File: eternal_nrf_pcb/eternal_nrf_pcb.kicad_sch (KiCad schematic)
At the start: 19 parts, among them U1 BQ25504

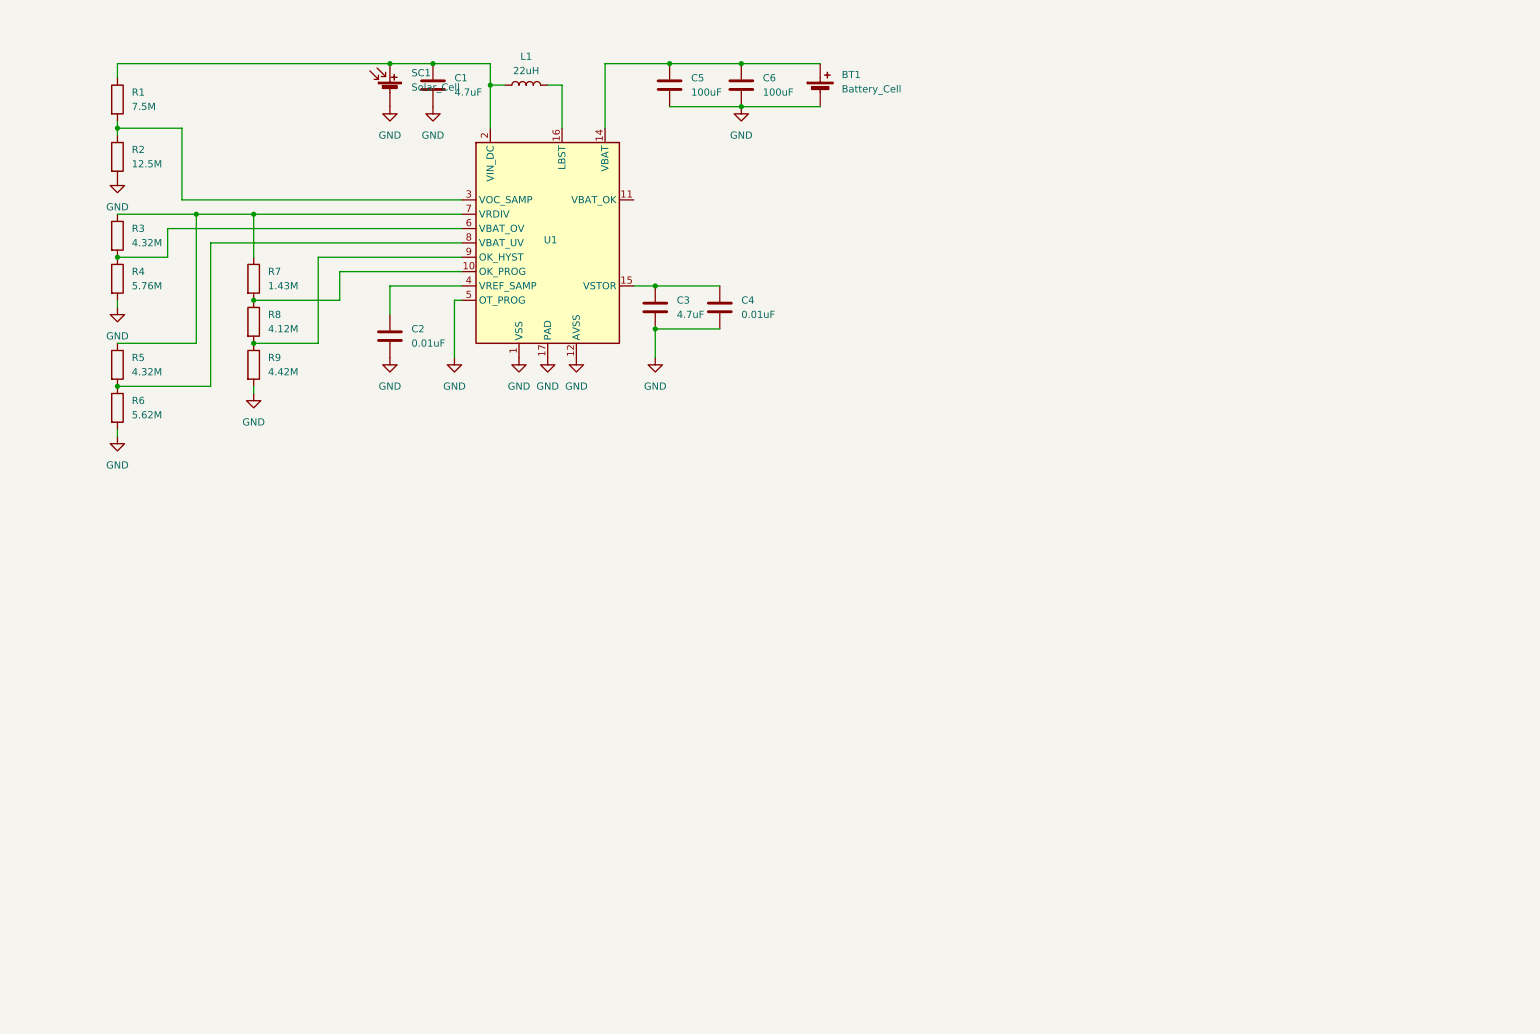
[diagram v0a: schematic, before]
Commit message: add nrf barebones schema
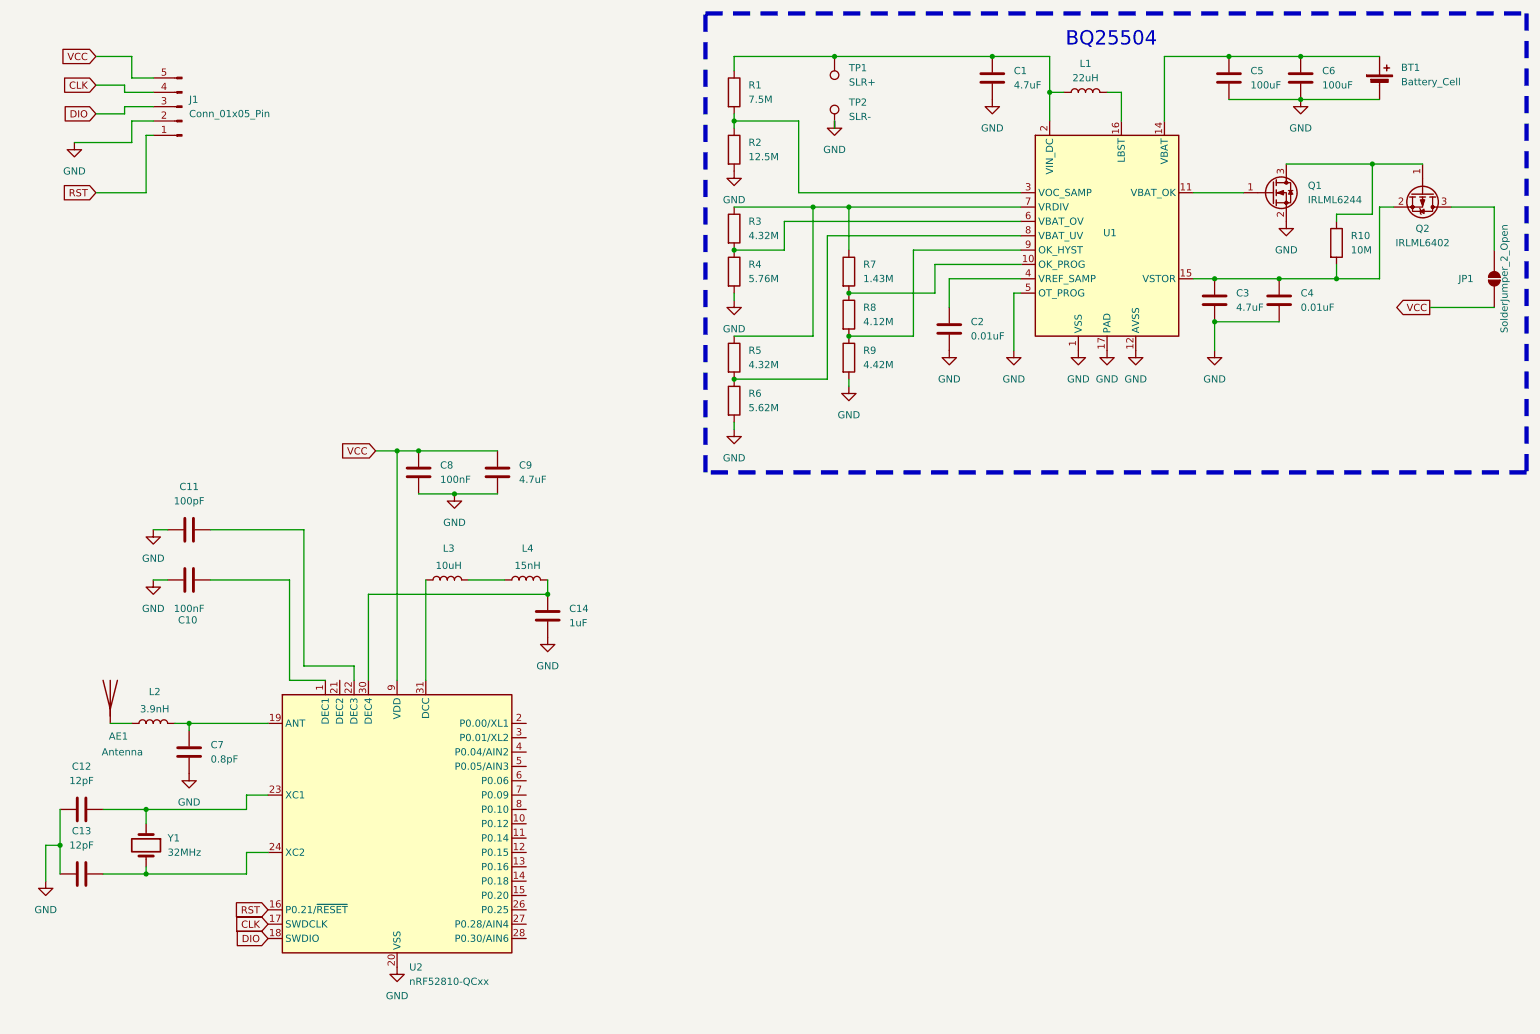
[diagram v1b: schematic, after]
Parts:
- removed SC1: Solar_Cell, symbol Device:Solar_Cell
- added AE1: Antenna, symbol Device:Antenna
- added C10, C8: 100nF, Capacitor_SMD:C_0402_1005Metric_Pad0.74x0.62mm_HandSolder, symbol Device:C
- added C11: 100pF, Capacitor_SMD:C_0402_1005Metric_Pad0.74x0.62mm_HandSolder, symbol Device:C
- added C12, C13: 12pF, Capacitor_SMD:C_0402_1005Metric_Pad0.74x0.62mm_HandSolder, symbol Device:C
- added C14: 1uF, Capacitor_SMD:C_0402_1005Metric_Pad0.74x0.62mm_HandSolder, symbol Device:C
- added C7: 0.8pF, Capacitor_SMD:C_0402_1005Metric_Pad0.74x0.62mm_HandSolder, symbol Device:C
- added C9: 4.7uF, Capacitor_SMD:C_0603_1608Metric_Pad1.08x0.95mm_HandSolder, symbol Device:C
- added J1: Conn_01x05_Pin, Connector_PinHeader_2.00mm:PinHeader_1x05_P2.00mm_Vertical, symbol Connector:Conn_01x05_Pin
- added JP1: SolderJumper_2_Open, Jumper:SolderJumper-2_P1.3mm_Open_TrianglePad1.0x1.5mm, symbol Jumper:SolderJumper_2_Open
- added L2: 3.9nH, Inductor_SMD:L_0402_1005Metric_Pad0.77x0.64mm_HandSolder, symbol Device:L
- added L3: 10uH, Inductor_SMD:L_0603_1608Metric_Pad1.05x0.95mm_HandSolder, symbol Device:L
- added L4: 15nH, Inductor_SMD:L_0402_1005Metric_Pad0.77x0.64mm_HandSolder, symbol Device:L
- added Q1: IRLML6244, Package_TO_SOT_SMD:SOT-23, symbol Transistor_FET:IRLML6244
- added Q2: IRLML6402, Package_TO_SOT_SMD:SOT-23, symbol Transistor_FET:IRLML6402
- added R10: 10M, Resistor_SMD:R_0603_1608Metric_Pad0.98x0.95mm_HandSolder, symbol Device:R
- added TP1: SLR+, TestPoint:TestPoint_Pad_D2.0mm, symbol Connector:TestPoint
- added TP2: SLR-, TestPoint:TestPoint_Pad_D2.0mm, symbol Connector:TestPoint
- added U2: nRF52810-QCxx, Package_DFN_QFN:QFN-32-1EP_5x5mm_P0.5mm_EP3.6x3.6mm, symbol MCU_Nordic:nRF52810-QCxx
- added Y1: 32MHz, symbol Device:Crystal
- BT1: footprint Battery:BatteryHolder_Keystone_3002_1x2032 -> Battery:BatteryHolder_Seiko_MS621F
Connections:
- net GND: now also C10.1, C11.1, C12.1, C13.1, C14.2, C7.2, C8.2, C9.2, J1.2 (Pin_2), Q1.2 (S), TP2.1, U2.20 (VSS), U2.29 (VSS), U2.33 (VSS)
- net at C3.1, C4.1, U1.15 (VSTOR): now also Q2.2 (S), R10.2
- net at C1.1, L1.1, R1.1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: now also TP1.1
- net at U1.11 (VBAT_OK): now also Q1.1 (G)
- new net: C12.2, U2.23 (XC1), Y1.1
- new net: C13.2, U2.24 (XC2), Y1.2
- new net: Q1.3 (D), Q2.1 (G), R10.1
- new net: AE1.1 (A), L2.1
- new net: C7.1, L2.2, U2.19 (ANT)
- new net: JP1.2 (B), Q2.3 (D)
- new net: C11.2, U2.22 (DEC3)
- new net: L3.2, L4.1
- new net: C14.1, L4.2, U2.30 (DEC4)
- new net: C10.2, U2.1 (DEC1)
- new net: L3.1, U2.31 (DCC)
- new net CLK: J1.4 (Pin_4), U2.17 (SWDCLK)
- new net DIO: J1.3 (Pin_3), U2.18 (SWDIO)
- new net RST: J1.1 (Pin_1), U2.16 (P0.21/~{RESET})
- new net VCC: C8.1, C9.1, J1.5 (Pin_5), JP1.1 (A), U2.25 (VDD), U2.32 (VDD), U2.9 (VDD)
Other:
- note added: "BQ25504"
- moved on the sheet: BT1, C1, C2, C3, C4, C5, C6, L1, R1, R2, R3, R4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

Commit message: add footprints
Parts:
- removed AE1: Antenna, symbol Device:Antenna
- removed Y1: 32MHz, symbol Device:Crystal
- added AE1: Antenna_Dipole, RF_Antenna:Johanson_2450AT18x100, symbol Device:Antenna_Dipole
- added Y1: Crystal_GND24, Crystal:Crystal_SMD_3225-4Pin_3.2x2.5mm, symbol Device:Crystal_GND24
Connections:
- net GND: now also J1.1 (Pin_1), Y1.2 (G), Y1.4 (G); no longer J1.2 (Pin_2)
- net RST: now also J1.2 (Pin_2); no longer J1.1 (Pin_1)
- net at C12.2, U2.23 (XC1): now also Y1.1
- net at C13.2, U2.24 (XC2): now also Y1.3
- net at L2.1: now also AE1.1
- no-connect marks 0 -> 1
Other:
- note added: "CONNECTOR"

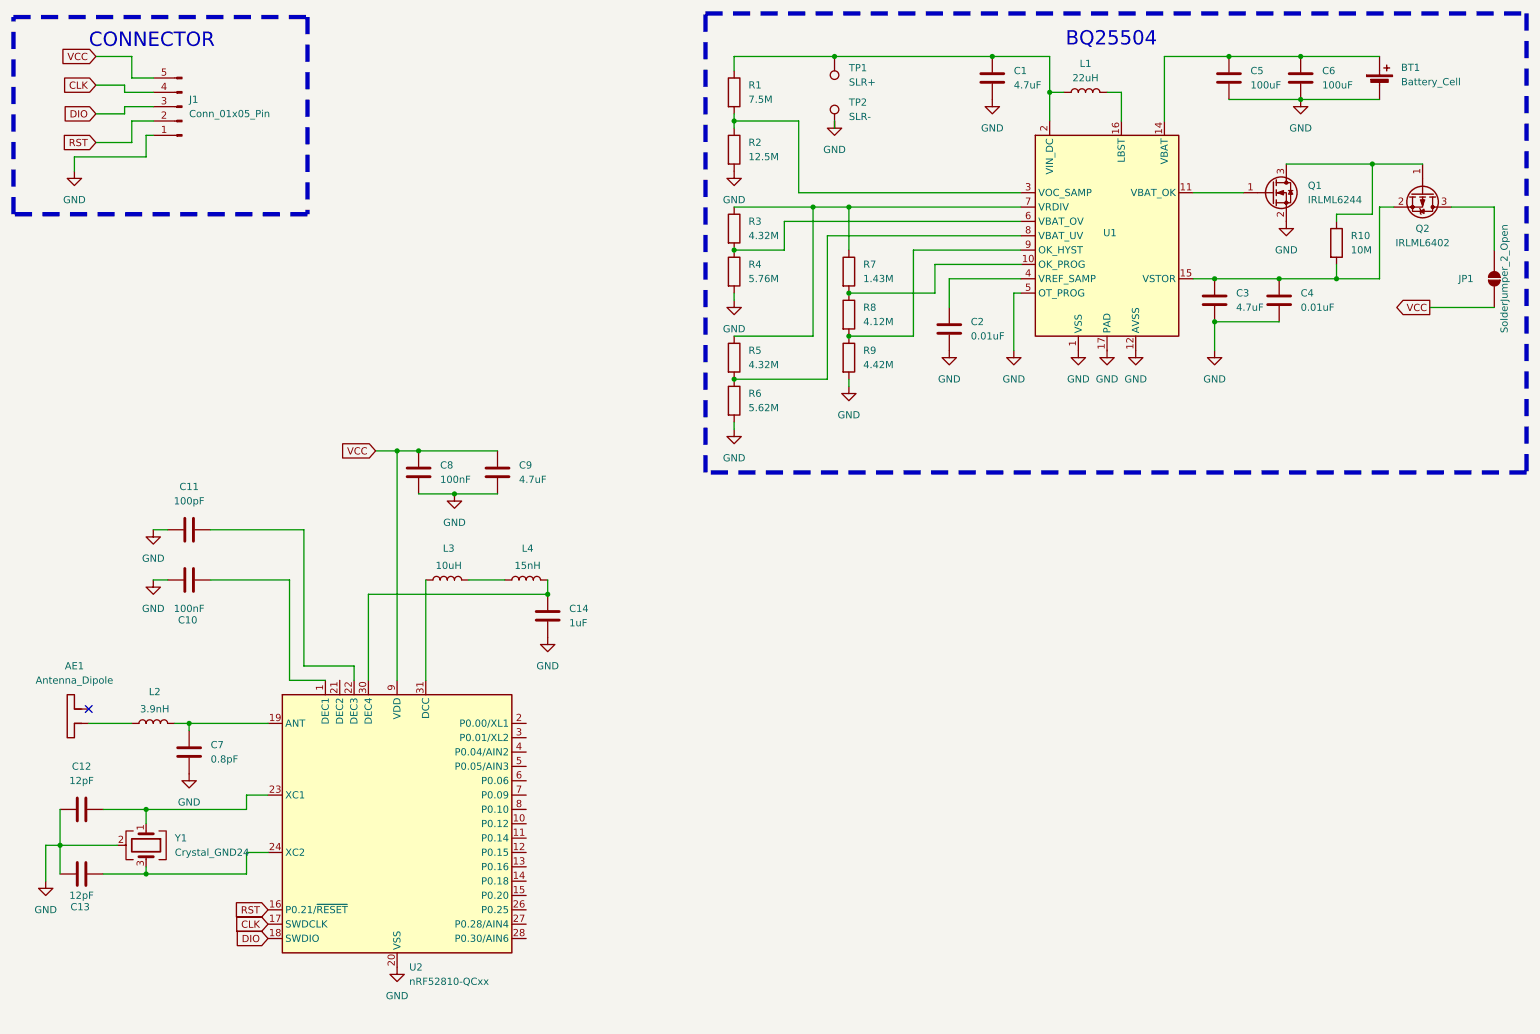
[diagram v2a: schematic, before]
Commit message: add button and led
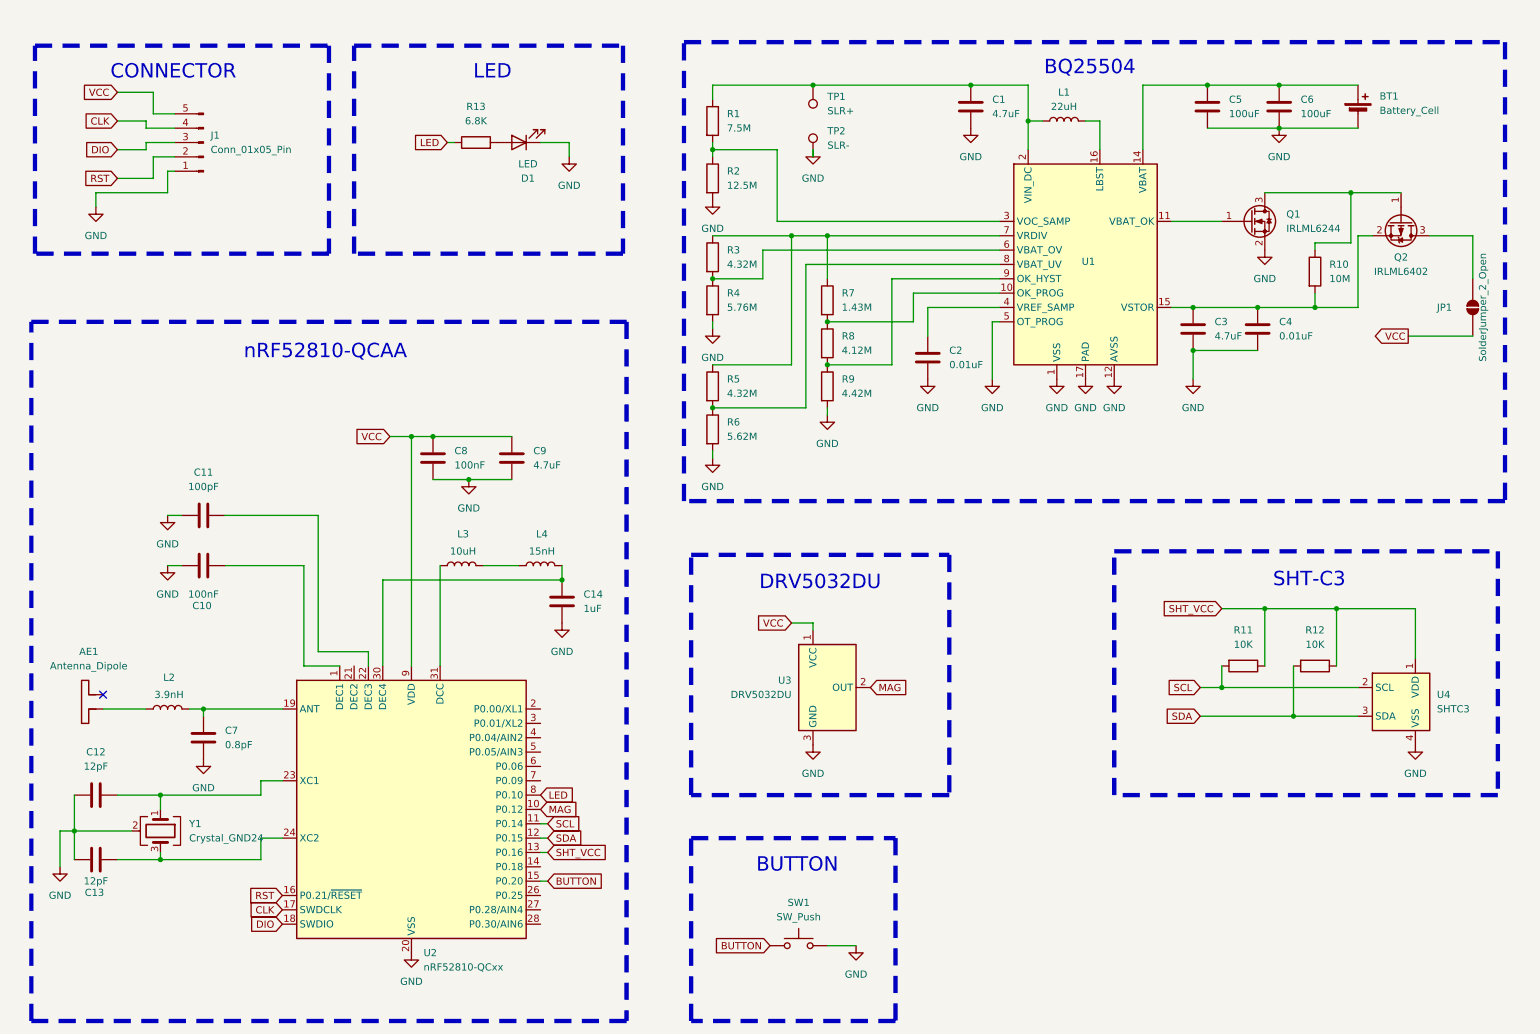
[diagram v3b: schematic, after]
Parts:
- added D1: LED, LED_SMD:LED_0603_1608Metric, symbol Device:LED
- added R11, R12: 10K, Resistor_SMD:R_0402_1005Metric_Pad0.72x0.64mm_HandSolder, symbol Device:R
- added R13: 6.8K, Resistor_SMD:R_0402_1005Metric_Pad0.72x0.64mm_HandSolder, symbol Device:R
- added SW1: SW_Push, symbol Switch:SW_Push
- added U3: DRV5032DU, Package_TO_SOT_SMD:SOT-23, symbol Sensor_Magnetic:DRV5033AJxDBZ
- added U4: SHTC3, Sensor_Humidity:Sensirion_DFN-4-1EP_2x2mm_P1mm_EP0.7x1.6mm, symbol Sensor_Humidity:SHTC3
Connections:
- net GND: now also D1.1 (K), SW1.2, U3.3 (GND), U4.4 (VSS)
- net VCC: now also U3.1 (VCC)
- net MAG: now reaches U2.10 (P0.12)
- net MAG: now also U3.2 (OUT)
- net SCL: now reaches U2.11 (P0.14)
- net SCL: now also R11.2, U4.2 (SCL)
- net SDA: now reaches U2.12 (P0.15)
- net SDA: now also R12.2, U4.3 (SDA)
- net SHT_VCC: now reaches U2.13 (P0.16)
- net SHT_VCC: now also R11.1, R12.1, U4.1 (VDD)
- net BUTTON: now reaches U2.15 (P0.20)
- net BUTTON: now also SW1.1
- net LED: now reaches U2.8 (P0.10)
- net LED: now also R13.1
- new net: D1.2 (A), R13.2
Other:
- note added: "BUTTON"
- note added: "DRV5032DU"
- note added: "LED"
- note added: "SHT-C3"
- note added: "nRF52810-QCAA"
- moved on the sheet: AE1, BT1, C1, C10, C11, C12, C13, C14, C2, C3, C4, C5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

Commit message: add footprint
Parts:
- SW1: footprint (none) -> TS-A002:TST-A002_0.6MM_BOSS
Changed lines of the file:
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@@
 			)
 		)
-		(property "Footprint" ""
+		(property "Footprint" "TS-A002:TST-A002_0.6MM_BOSS"
 			(at 153.67 173.99 0)
 			(hide yes)

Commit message: place parts
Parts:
- added C15: 1uF, Capacitor_SMD:C_0402_1005Metric_Pad0.74x0.62mm_HandSolder, symbol Device:C
- added C16, C17: 100uF, Capacitor_SMD:C_1210_3225Metric, symbol Device:C
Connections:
- net GND: now also C15.2, C16.2, C17.2
- net SHT_VCC: now also C15.1
- net at BT1.1 (+), C5.1, C6.1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: now also C16.1, C17.1
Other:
- moved on the sheet: R11, R12, U4

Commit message: almost final layout
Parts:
- added C18, C19: 100uF, Capacitor_SMD:C_1210_3225Metric, symbol Device:C
- added L5: 6.8uH, Inductor_SMD:L_0402_1005Metric_Pad0.77x0.64mm_HandSolder, symbol Device:L
- AE1: value Antenna_Dipole -> RFANT3216120A5T
- BT1: value Battery_Cell -> Battery
- J1: footprint Connector_PinHeader_2.00mm:PinHeader_1x05_P2.00mm_Vertical -> Connector_PinHeader_2.54mm:PinHeader_1x05_P2.54mm_Vertical
- R13: value 6.8K -> 4.7K
- R4: value 5.76M -> 6.34M
- TP1: value SLR+ -> S+
- TP2: value SLR- -> S-
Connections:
- net GND: now also C18.2, C19.2
- net at BT1.1 (+), C16.1, C17.1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: now also C18.1, C19.1
- net at L2.1: now also L5.2; no longer AE1.1
- new net: AE1.1, L5.1
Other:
- moved on the sheet: AE1, BT1, L2

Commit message: update sheet info
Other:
- company: (none) -> Madhukar Temba
- title: (none) -> Eternal nRF
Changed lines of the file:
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@@
 	(generator_version "10.0")
 	(paper "A4")
+	(title_block
+		(title "Eternal nRF")
+		(date "2026-05-09")
+		(rev "1")
+		(company "Madhukar Temba")
+	)
 	(rectangle
 		(start 198.755 109.22)

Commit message: complete board
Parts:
- removed J1: Conn_01x05_Pin, Connector_PinHeader_2.54mm:PinHeader_1x05_P2.54mm_Vertical, symbol Connector:Conn_01x05_Pin
- added C20, C21: 22pF, Capacitor_SMD:C_0402_1005Metric_Pad0.74x0.62mm_HandSolder, symbol Device:C
- added J1: Conn_01x07_Pin, Connector_PinHeader_2.54mm:PinHeader_1x07_P2.54mm_Vertical, symbol Connector:Conn_01x07_Pin
- added Y2: Crystal, Crystal:Crystal_SMD_3215-2Pin_3.2x1.5mm, symbol Device:Crystal
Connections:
- net CLK: now also J1.6 (Pin_6)
- net DIO: now also J1.5 (Pin_5)
- net GND: now also C20.1, C21.2, J1.1 (Pin_1)
- net RST: now also J1.4 (Pin_4)
- net VCC: now also J1.7 (Pin_7)
- net at U2.2 (P0.00/XL1): now also C21.1, Y2.2
- net at U2.3 (P0.01/XL2): now also C20.2, Y2.1
- net TX: now reaches U2.4 (P0.04/AIN2)
- net TX: now also J1.2 (Pin_2)
- net RX: now reaches U2.5 (P0.05/AIN3)
- net RX: now also J1.3 (Pin_3)
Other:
- moved on the sheet: C15, R11, R12, SW1, U3, U4
